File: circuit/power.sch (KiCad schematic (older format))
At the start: 0 parts

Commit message: Added microcontroller circuit
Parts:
- added C19, C20: 10µF, Capacitor_SMD:C_0805_2012Metric_Pad1.15x1.40mm_HandSolder, symbol Device:C
- added U56: LM1117-3.3, Package_TO_SOT_SMD:SOT-223-3_TabPin2, symbol Regulator_Linear:LM1117-3.3
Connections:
- new net +3V3: C20.1, U56.2 (VO)
- new net +5V: C19.1, U56.3 (VI)
- new net GND: C19.2, C20.2, U56.1 (GND)
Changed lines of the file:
@@
 $Descr A4 11693 8268
 encoding utf-8
-Sheet 5 21
+Sheet 4 21
 Title ""
 Date ""
@@
 Comment4 ""
 $EndDescr
+$Comp
+L power:GND #PWR0146
+U 1 1 5E3AFB76
+P 4750 3850
+F 0 "#PWR0146" H 4750 3600 50  0001 C CNN
+F 1 "GND" H 4755 3677 50  0000 C CNN
+F 2 "" H 4750 3850 50  0001 C CNN
+F 3 "" H 4750 3850 50  0001 C CNN
+	1    4750 3850
+	1    0    0    -1
+$EndComp
+Wire Wire Line
+	4750 3850 4750 3750
+$Comp
+L power:+5V #PWR0147
+U 1 1 5E3B05AF
+P 4300 3150
+F 0 "#PWR0147" H 4300 3000 50  0001 C CNN
+F 1 "+5V" H 4315 3323 50  0000 C CNN
+F 2 "" H 4300 3150 50  0001 C CNN
+F 3 "" H 4300 3150 50  0001 C CNN
+	1    4300 3150
+	1    0    0    -1
+$EndComp
+Wire Wire Line
+	4300 3150 4300 3350
+Wire Wire Line
+	4300 3350 4450 3350
+$Comp
+L power:+3.3V #PWR0148
+U 1 1 5E3B1B9A
+P 5200 3150
+F 0 "#PWR0148" H 5200 3000 50  0001 C CNN
+F 1 "+3.3V" H 5215 3323 50  0000 C CNN
+F 2 "" H 5200 3150 50  0001 C CNN
+F 3 "" H 5200 3150 50  0001 C CNN
+	1    5200 3150
+	1    0    0    -1
+$EndComp
+Wire Wire Line
+	5200 3150 5200 3350
+Wire Wire Line
+	5200 3350 5050 3350
+$Comp
+L Regulator_Linear:LM1117-3.3 U56
+U 1 1 5E3B2541
+P 4750 3350
+F 0 "U56" H 4750 3592 50  0000 C CNN
+F 1 "LM1117-3.3" H 4750 3501 50  0000 C CNN
+F 2 "Package_TO_SOT_SMD:SOT-223-3_TabPin2" H 4750 3350 50  0001 C CNN
+F 3 "http://www.ti.com/lit/ds/symlink/lm1117.pdf" H 4750 3350 50  0001 C CNN
+	1    4750 3350
+	1    0    0    -1
+$EndComp
+$Comp
+L Device:C C19
+U 1 1 5E3B2D24
+P 4300 3600
+F 0 "C19" H 4415 3646 50  0000 L CNN
+F 1 "10µF" H 4415 3555 50  0000 L CNN
+F 2 "Capacitor_SMD:C_0805_2012Metric_Pad1.15x1.40mm_HandSolder" H 4338 3450 50  0001 C CNN
+F 3 "~" H 4300 3600 50  0001 C CNN
+	1    4300 3600
+	1    0    0    -1
+$EndComp
+Wire Wire Line
+	4300 3450 4300 3350
+Connection ~ 4300 3350
+Wire Wire Line
+	4300 3750 4750 3750
+Connection ~ 4750 3750
+Wire Wire Line
+	4750 3750 4750 3650
+$Comp
+L Device:C C20
+U 1 1 5E3B357E
+P 5200 3600
+F 0 "C20" H 5315 3646 50  0000 L CNN
+F 1 "10µF" H 5315 3555 50  0000 L CNN
+F 2 "Capacitor_SMD:C_0805_2012Metric_Pad1.15x1.40mm_HandSolder" H 5238 3450 50  0001 C CNN
+F 3 "~" H 5200 3600 50  0001 C CNN
+	1    5200 3600
+	1    0    0    -1
+$EndComp
+Wire Wire Line
+	5200 3450 5200 3350
+Connection ~ 5200 3350
+Wire Wire Line
+	5200 3750 4750 3750
+Wire Wire Line
+	2600 3350 2600 3150
+Wire Wire Line
+	3400 3350 3400 3150
+$Comp
+L power:GND #PWR03
+U 1 1 5E3D721F
+P 3400 3350
+F 0 "#PWR03" H 3400 3100 50  0001 C CNN
+F 1 "GND" H 3405 3177 50  0000 C CNN
+F 2 "" H 3400 3350 50  0001 C CNN
+F 3 "" H 3400 3350 50  0001 C CNN
+	1    3400 3350
+	1    0    0    -1
+$EndComp
+$Comp
+L power:+5V #PWR01
+U 1 1 5E3D5F41
+P 2600 3350
+F 0 "#PWR01" H 2600 3200 50  0001 C CNN
+F 1 "+5V" H 2615 3523 50  0000 C CNN
+F 2 "" H 2600 3350 50  0001 C CNN
+F 3 "" H 2600 3350 50  0001 C CNN
+	1    2600 3350
+	-1   0    0    1
+$EndComp
+$Comp
+L power:PWR_FLAG #FLG01
+U 1 1 5E3D5C5B
+P 2600 3150
+F 0 "#FLG01" H 2600 3225 50  0001 C CNN
+F 1 "PWR_FLAG" H 2600 3323 50  0000 C CNN
+F 2 "" H 2600 3150 50  0001 C CNN
+F 3 "~" H 2600 3150 50  0001 C CNN
+	1    2600 3150
+	1    0    0    -1
+$EndComp
+$Comp
+L power:PWR_FLAG #FLG03
+U 1 1 5E3D58C0
+P 3400 3150
+F 0 "#FLG03" H 3400 3225 50  0001 C CNN
+F 1 "PWR_FLAG" H 3400 3323 50  0000 C CNN
+F 2 "" H 3400 3150 50  0001 C CNN
+F 3 "~" H 3400 3150 50  0001 C CNN
+	1    3400 3150
+	1    0    0    -1
+$EndComp
 $EndSCHEMATC

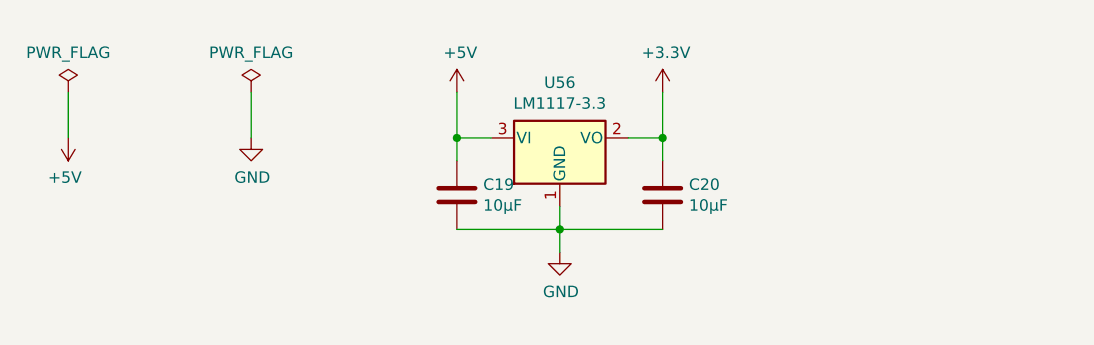
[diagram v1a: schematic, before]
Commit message: Added usb power connector
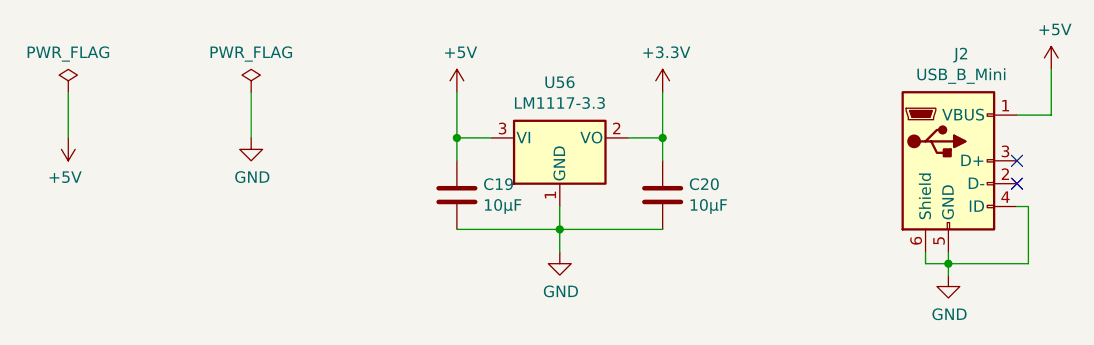
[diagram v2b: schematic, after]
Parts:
- added J2: USB_B_Mini, Connector_USB:USB_Mini-B_Lumberg_2486_01_Horizontal, symbol Connector:USB_B_Mini
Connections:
- net +5V: now also J2.1 (VBUS)
- net GND: now also J2.4 (ID), J2.5 (GND), J2.6 (Shield)
- no-connect marks 0 -> 2
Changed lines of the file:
@@
 	1    0    0    -1
 $EndComp
+$Comp
+L Connector:USB_B_Mini J2
+U 1 1 5E52D034
+P 6450 3450
+F 0 "J2" H 6507 3917 50  0000 C CNN
+F 1 "USB_B_Mini" H 6507 3826 50  0000 C CNN
+F 2 "Connector_USB:USB_Mini-B_Lumberg_2486_01_Horizontal" H 6600 3400 50  0001 C CNN
+F 3 "~" H 6600 3400 50  0001 C CNN
+	1    6450 3450
+	1    0    0    -1
+$EndComp
+$Comp
+L power:+5V #PWR04
+U 1 1 5E52DFB6
+P 6900 3050
+F 0 "#PWR04" H 6900 2900 50  0001 C CNN
+F 1 "+5V" H 6915 3223 50  0000 C CNN
+F 2 "" H 6900 3050 50  0001 C CNN
+F 3 "" H 6900 3050 50  0001 C CNN
+	1    6900 3050
+	1    0    0    -1
+$EndComp
+Wire Wire Line
+	6900 3050 6900 3250
+Wire Wire Line
+	6900 3250 6750 3250
+$Comp
+L power:GND #PWR02
+U 1 1 5E52EC7B
+P 6450 3950
+F 0 "#PWR02" H 6450 3700 50  0001 C CNN
+F 1 "GND" H 6455 3777 50  0000 C CNN
+F 2 "" H 6450 3950 50  0001 C CNN
+F 3 "" H 6450 3950 50  0001 C CNN
+	1    6450 3950
+	1    0    0    -1
+$EndComp
+Wire Wire Line
+	6450 3850 6450 3900
+Wire Wire Line
+	6450 3900 6800 3900
+Wire Wire Line
+	6800 3900 6800 3650
+Wire Wire Line
+	6800 3650 6750 3650
+Connection ~ 6450 3900
+Wire Wire Line
+	6450 3900 6450 3950
+NoConn ~ 6750 3450
+NoConn ~ 6750 3550
+Wire Wire Line
+	6350 3850 6350 3900
+Wire Wire Line
+	6350 3900 6450 3900
 $EndSCHEMATC
